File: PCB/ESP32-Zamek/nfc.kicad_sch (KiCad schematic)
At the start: 18 parts

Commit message: NFC - znaleziono dokumentację projektową xD
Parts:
- removed Y?: 27.12 MHz, symbol Device:Crystal
- added C4, C5: C, symbol Device:C
- added R5, R6: R, symbol Device:R
- added Y2: XRCGB27M120F3A00R0, ourFootprints:XRCGB, symbol Device:Crystal_GND24
- C? (x2): value C -> 6pF
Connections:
- net +3.3V: now also IC?.10 (VEN), IC?.12 (VBAT2), IC?.13 (VDD(UP)), IC?.14 (VDD(TX)), IC?.17 (VDD(VMID)), IC?.28 (VBAT)
- net GND: now also IC?.20 (VSS(TX))
- net NFC_XTAL1: now also Y2.1
- net NFC_XTAL2: now also Y2.3
- net at C?.1, C?.1, L?.2: now also R6.1
- net at C?.1, C?.2, L?.2: now also R5.2
- net RXN: now reaches IC?.15 (RXN)
- net RXN: now also C4.2
- net RXP: now reaches IC?.16 (RXP)
- net RXP: now also C5.1
- new net: C5.2, R5.1
- new net: C4.1, R6.2
- no-connect marks 8 -> 11
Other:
- moved on the sheet: AE?, C?, IC?, L?, R?

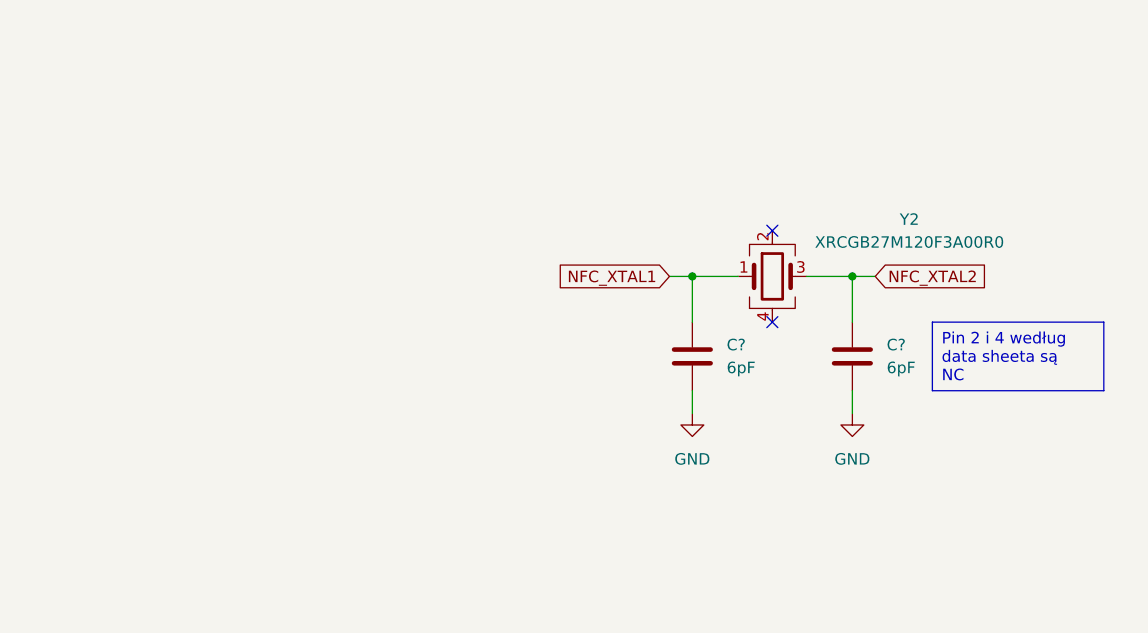
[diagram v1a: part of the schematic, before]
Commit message: Booting/Reset circuit change
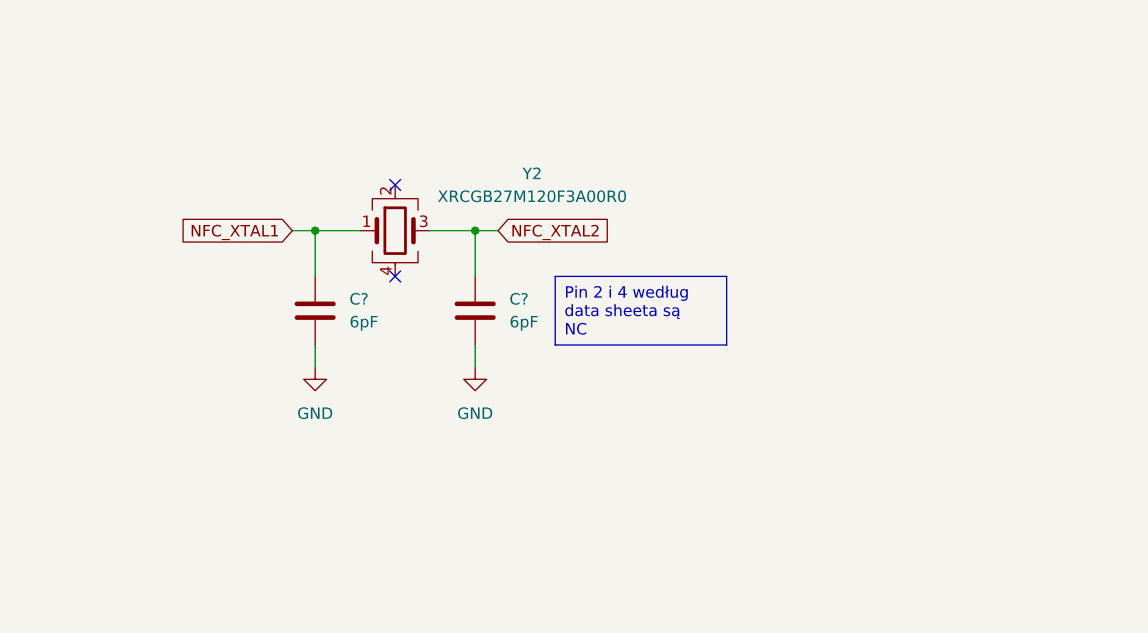
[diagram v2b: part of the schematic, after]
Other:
- moved on the sheet: C?, Y2
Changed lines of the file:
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@@
 	)
 	(junction
-		(at 237.49 143.51)
+		(at 195.58 138.43)
 		(diameter 0)
 		(color 0 0 0 0)
 	)
 	(junction
-		(at 255.27 143.51)
+		(at 213.36 138.43)
 		(diameter 0)
 		(color 0 0 0 0)
 	)
 	(no_connect
-		(at 246.38 138.43)
+		(at 204.47 133.35)
 	)
 	(no_connect
-		(at 246.38 148.59)
+		(at 204.47 143.51)
 	)
 	(no_connect
@@
 	(wire
 		(pts
-			(xy 255.27 143.51) (xy 257.81 143.51)
+			(xy 213.36 138.43) (xy 215.9 138.43)
 		)
 		(stroke
@@
 	(wire
 		(pts
-			(xy 250.19 143.51) (xy 255.27 143.51)
+			(xy 208.28 138.43) (xy 213.36 138.43)
 		)
 		(stroke
@@
 	(wire
 		(pts
-			(xy 237.49 143.51) (xy 242.57 143.51)
+			(xy 195.58 138.43) (xy 200.66 138.43)
 		)
 		(stroke
@@
 	(wire
 		(pts
-			(xy 237.49 156.21) (xy 237.49 158.75)
+			(xy 195.58 151.13) (xy 195.58 153.67)
 		)
 		(stroke
@@
 	(wire
 		(pts
-			(xy 255.27 143.51) (xy 255.27 148.59)
+			(xy 213.36 138.43) (xy 213.36 143.51)
 		)
 		(stroke
@@
 	(wire
 		(pts
-			(xy 255.27 156.21) (xy 255.27 158.75)
+			(xy 213.36 151.13) (xy 213.36 153.67)
 		)
 		(stroke
@@
 	(wire
 		(pts
-			(xy 234.95 143.51) (xy 237.49 143.51)
+			(xy 193.04 138.43) (xy 195.58 138.43)
 		)
 		(stroke
@@
 	(wire
 		(pts
-			(xy 237.49 148.59) (xy 237.49 143.51)
+			(xy 195.58 143.51) (xy 195.58 138.43)
 		)
 		(stroke
@@
 	(text_box "Pin 2 i 4 według data sheeta są NC"
 		(exclude_from_sim no)
-		(at 264.16 148.59 0)
+		(at 222.25 143.51 0)
 		(size 19.05 7.62)
 		(stroke
@@
 	(global_label "NFC_XTAL2"
 		(shape input)
-		(at 257.81 143.51 0)
+		(at 215.9 138.43 0)
 		(fields_autoplaced yes)
 		(effects
@@
 		)
 		(property "Intersheetrefs" "${INTERSHEET_REFS}"
-			(at 270.9552 143.51 0)
+			(at 229.0452 138.43 0)
 			(effects
 				(font
@@
 	(global_label "NFC_XTAL1"
 		(shape input)
-		(at 234.95 143.51 180)
+		(at 193.04 138.43 180)
 		(fields_autoplaced yes)
 		(effects
@@
 		)
 		(property "Intersheetrefs" "${INTERSHEET_REFS}"
-			(at 221.8048 143.51 0)
+			(at 179.8948 138.43 0)
 			(effects
 				(font
@@
 	(symbol
 		(lib_id "power:GND")
-		(at 237.49 158.75 0)
+		(at 195.58 153.67 0)
 		(unit 1)
 		(exclude_from_sim no)
@@
 		(fields_autoplaced yes)
 		(property "Reference" "#PWR022"
-			(at 237.49 165.1 0)
+			(at 195.58 160.02 0)
 			(effects
 				(font
@@
 		)
 		(property "Value" "GND"
-			(at 237.49 163.83 0)
+			(at 195.58 158.75 0)
 			(effects
 				(font
@@
 		)
 		(property "Footprint" ""
-			(at 237.49 158.75 0)
+			(at 195.58 153.67 0)
 			(effects
 				(font
@@
 		)
 		(property "Datasheet" ""
-			(at 237.49 158.75 0)
+			(at 195.58 153.67 0)
 			(effects
 				(font
@@
 		)
 		(property "Description" "Power symbol creates a global label with name \"GND\" , ground"
-			(at 237.49 158.75 0)
+			(at 195.58 153.67 0)
 			(effects
 				(font
@@
 	(symbol
 		(lib_id "Device:C")
-		(at 237.49 152.4 0)
+		(at 195.58 147.32 0)
 		(unit 1)
 		(exclude_from_sim no)
@@
 		(fields_autoplaced yes)
 		(property "Reference" "C?"
-			(at 241.3 151.1299 0)
+			(at 199.39 146.0499 0)
 			(effects
 				(font
@@
 		)
 		(property "Value" "6pF"
-			(at 241.3 153.6699 0)
+			(at 199.39 148.5899 0)
 			(effects
 				(font
@@
 		)
 		(property "Footprint" ""
-			(at 238.4552 156.21 0)
+			(at 196.5452 151.13 0)
 			(effects
 				(font
@@
 		)
 		(property "Datasheet" "~"
-			(at 237.49 152.4 0)
+			(at 195.58 147.32 0)
 			(effects
 				(font
@@
 		)
 		(property "Description" "Unpolarized capacitor"
-			(at 237.49 152.4 0)
+			(at 195.58 147.32 0)
 			(effects
 				(font
@@
 	(symbol
 		(lib_id "Device:Crystal_GND24")
-		(at 246.38 143.51 0)
+		(at 204.47 138.43 0)
 		(unit 1)
 		(exclude_from_sim no)
@@
 		(fields_autoplaced yes)
 		(property "Reference" "Y2"
-			(at 261.62 137.1914 0)
+			(at 219.71 132.1114 0)
 			(effects
 				(font
@@
 		)
 		(property "Value" "XRCGB27M120F3A00R0"
-			(at 261.62 139.7314 0)
+			(at 219.71 134.6514 0)
 			(effects
 				(font
@@
 		)
 		(property "Footprint" "ourFootprints:XRCGB"
-			(at 246.38 143.51 0)
+			(at 204.47 138.43 0)
 			(effects
 				(font
@@
 		)
 		(property "Datasheet" "~"
-			(at 246.38 143.51 0)
+			(at 204.47 138.43 0)
 			(effects
 				(font
@@
 		)
 		(property "Description" "Four pin crystal, GND on pins 2 and 4"
-			(at 246.38 143.51 0)
+			(at 204.47 138.43 0)
 			(effects
 				(font
@@
 	(symbol
 		(lib_id "Device:C")
-		(at 255.27 152.4 0)
+		(at 213.36 147.32 0)
 		(unit 1)
 		(exclude_from_sim no)
@@
 		(fields_autoplaced yes)
 		(property "Reference" "C?"
-			(at 259.08 151.1299 0)
+			(at 217.17 146.0499 0)
 			(effects
 				(font
@@
 		)
 		(property "Value" "6pF"
-			(at 259.08 153.6699 0)
+			(at 217.17 148.5899 0)
 			(effects
 				(font
@@
 		)
 		(property "Footprint" ""
-			(at 256.2352 156.21 0)
+			(at 214.3252 151.13 0)
 			(effects
 				(font
@@
 		)
 		(property "Datasheet" "~"
-			(at 255.27 152.4 0)
+			(at 213.36 147.32 0)
 			(effects
 				(font
@@
 		)
 		(property "Description" "Unpolarized capacitor"
-			(at 255.27 152.4 0)
+			(at 213.36 147.32 0)
 			(effects
 				(font
@@
 	(symbol
 		(lib_id "power:GND")
-		(at 255.27 158.75 0)
+		(at 213.36 153.67 0)
 		(unit 1)
 		(exclude_from_sim no)
@@
 		(fields_autoplaced yes)
 		(property "Reference" "#PWR023"
-			(at 255.27 165.1 0)
+			(at 213.36 160.02 0)
 			(effects
 				(font
@@
 		)
 		(property "Value" "GND"
-			(at 255.27 163.83 0)
+			(at 213.36 158.75 0)
 			(effects
 				(font
@@
 		)
 		(property "Footprint" ""
-			(at 255.27 158.75 0)
+			(at 213.36 153.67 0)
 			(effects
 				(font
@@
 		)
 		(property "Datasheet" ""
-			(at 255.27 158.75 0)
+			(at 213.36 153.67 0)
 			(effects
 				(font
@@
 		)
 		(property "Description" "Power symbol creates a global label with name \"GND\" , ground"
-			(at 255.27 158.75 0)
+			(at 213.36 153.67 0)
 			(effects
 				(font

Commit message: Add the nfc connector with external outputs
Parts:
- removed AE?: Antenna_Loop, symbol Device:Antenna_Loop
- removed C4, C5, C? (x7): C, symbol Device:C
- removed C? (x2): 6pF, symbol Device:C
- removed IC?: PN7160A1HN_C100E, QFN50P600X600X100-41N-D, symbol PN7160A1HN_C100E:PN7160A1HN_C100E
- removed L? (x2): L, symbol Device:L
- removed R5, R6, R? (x4): R, symbol Device:R
- removed Y2: XRCGB27M120F3A00R0, ourFootprints:XRCGB, symbol Device:Crystal_GND24
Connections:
- no-connect marks 11 -> 0
